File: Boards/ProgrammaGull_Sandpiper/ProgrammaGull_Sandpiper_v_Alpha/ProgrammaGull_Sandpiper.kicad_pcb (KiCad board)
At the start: 4 copper layers, 100 x 75 mm, 191 parts, among them J4 Conn_01x22_Socket, P1 USB_C_Plug_USB2.0, Q1 MMBT2907, Q2 MMBT2907, Q3 MMBT2907, Q4 MMBT2907, Q5 MMBT2907, Q6 MMBT2907, Q7 MMBT2907, Q8 MMBT2907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

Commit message: Converted to 3v3 7 segment drive voltage
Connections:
- Q1 pad 2: +5V -> +3V3
- Q2 pad 2: +5V -> +3V3
- Q3 pad 2: +5V -> +3V3
- Q4 pad 2: +5V -> +3V3
- Q5 pad 2: +5V -> +3V3
- Q6 pad 2: +5V -> +3V3
- Q7 pad 2: +5V -> +3V3
- Q8 pad 2: +5V -> +3V3
- R67 pad 2: +5V -> +3V3
- R68 pad 2: +5V -> +3V3
- R69 pad 2: +5V -> +3V3
- R70 pad 2: +5V -> +3V3
- R71 pad 2: +5V -> +3V3
- R72 pad 2: +5V -> +3V3
- R73 pad 2: +5V -> +3V3
- R74 pad 2: +5V -> +3V3
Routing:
- net +5V: track 88.9 -> 50.2 mm, vias 9 -> 0
- net +3V3: track 133.4 -> 149.2 mm, vias 56 -> 64
- removed copper zone on In1.Cu, net +5V

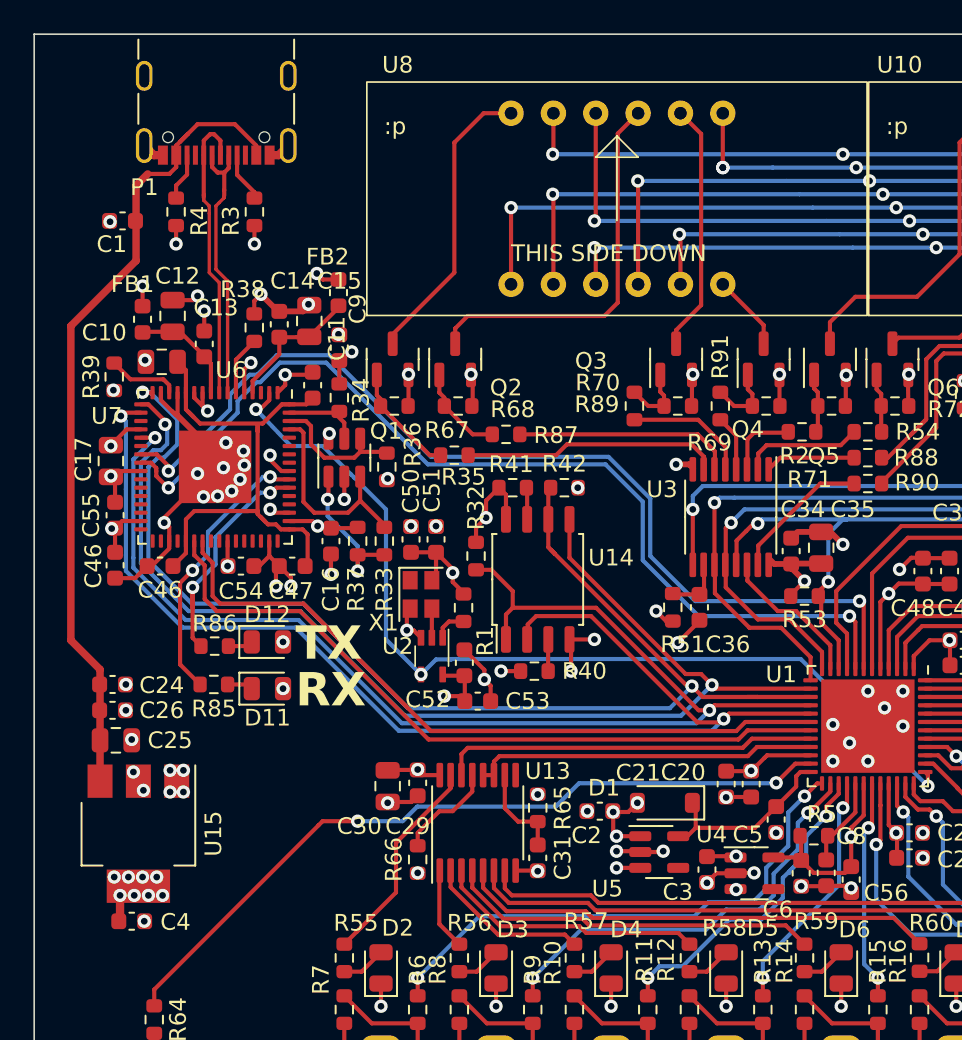
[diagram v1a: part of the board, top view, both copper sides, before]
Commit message: Sandpiper Alpha Schematic updated for new 7 segment drive strategy
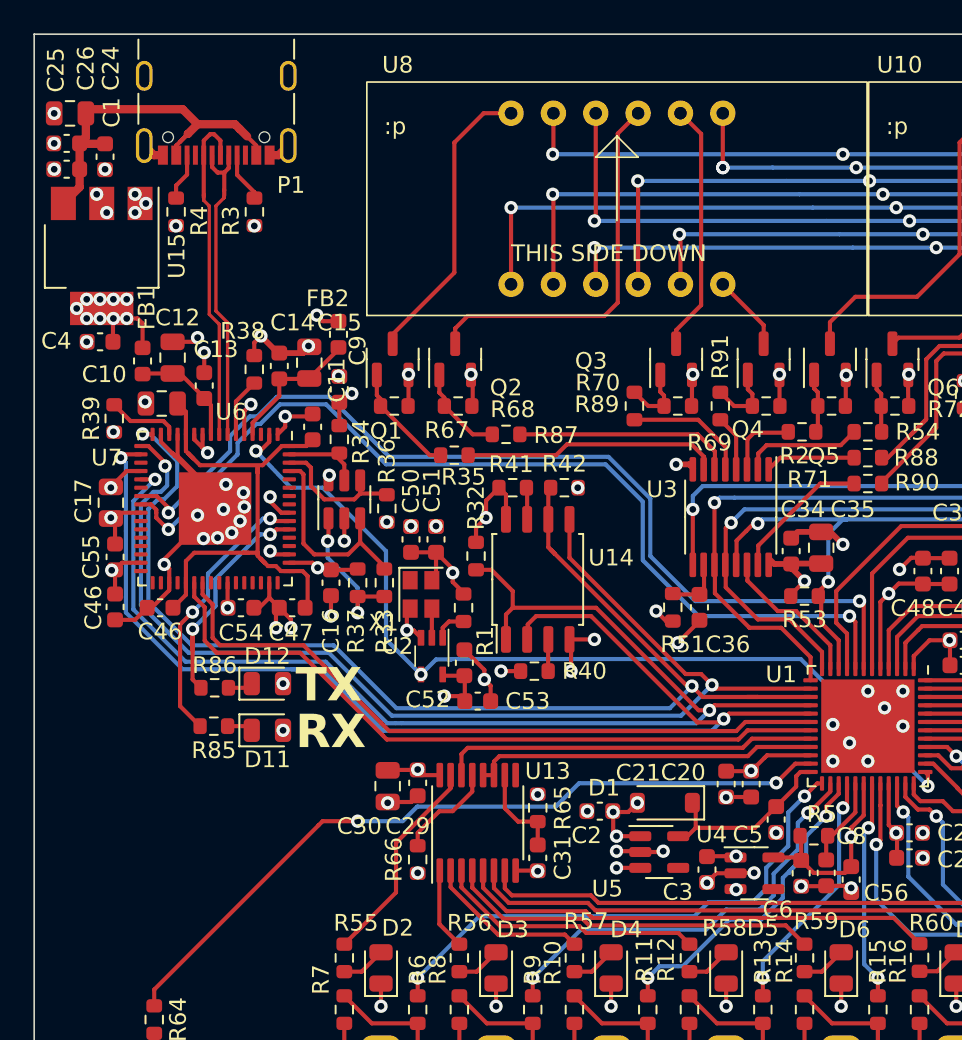
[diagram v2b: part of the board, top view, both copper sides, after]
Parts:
- R2, R35, R54, R87, R88, R89, R90, R91: value 680R -> 2k2
- R43, R44, R45, R46, R47, R48, R49, R50: value 383R -> 150R
- moved C25 37.7 mm to (27.1, 29.8), turned to 180 degrees
- moved C4 34.8 mm to (28.9, 43.5), turned to 180 degrees
- moved U15 34.7 mm to (29.1, 38.3)
- moved C26 34.1 mm to (26.9, 31.6), turned to 180 degrees
- moved C24 31.0 mm to (26.9, 33.1), turned to 180 degrees
- moved C1 3.99 mm to (29.2, 32.4), turned to -90 degrees
- moved C10 2.50 mm to (32.6, 47.1)
- moved C11 2.50 mm to (41.7, 48.5)
- moved C12 2.50 mm to (33.3, 44.4)
- moved C13 2.50 mm to (35.2, 46.1)
- moved C14 2.50 mm to (39.7, 44.9)
- moved C15 2.50 mm to (41.5, 44.7)
- moved C16 2.50 mm to (42.8, 57.9)
- moved C17 2.50 mm to (29.6, 53.1)
- moved C46 2.50 mm to (29.9, 59.4)
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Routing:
- net +5V: track 50.2 -> 23.8 mm
- net +3V3: track 149.2 -> 153.8 mm
- net /USB_D-: track 16.9 -> 19.4 mm
- net /USB_D+: track 17.9 -> 20.4 mm
- net /CLK_12M: track 57.6 -> 55.1 mm
- net GND: track 114.3 -> 112.2 mm, vias 94 -> 93
- net /UP5K_CDONE: track 59.7 -> 58.7 mm
- net /UP5K_UART_TX: track 43.0 -> 42.0 mm
- net /UP5K_CRESET: track 58.8 -> 57.8 mm
- net /FLASH_MOSI: track 70.4 -> 69.4 mm
- net /FLASH_CS: track 74.3 -> 73.3 mm
- net /UP5K_UART_RX: track 43.8 -> 42.8 mm
- net /FLASH_SCK: track 74.1 -> 73.1 mm
- net /FLASH_MISO: track 71.8 -> 70.9 mm
